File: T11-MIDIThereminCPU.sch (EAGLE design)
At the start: 62 parts, among them IC1 UA78M05DCY, IC4 QUAD_OPAMPD, IC5 4069D, J1 DCJ0202, Q1 16MHz, U1 ATMEGA328P-AU

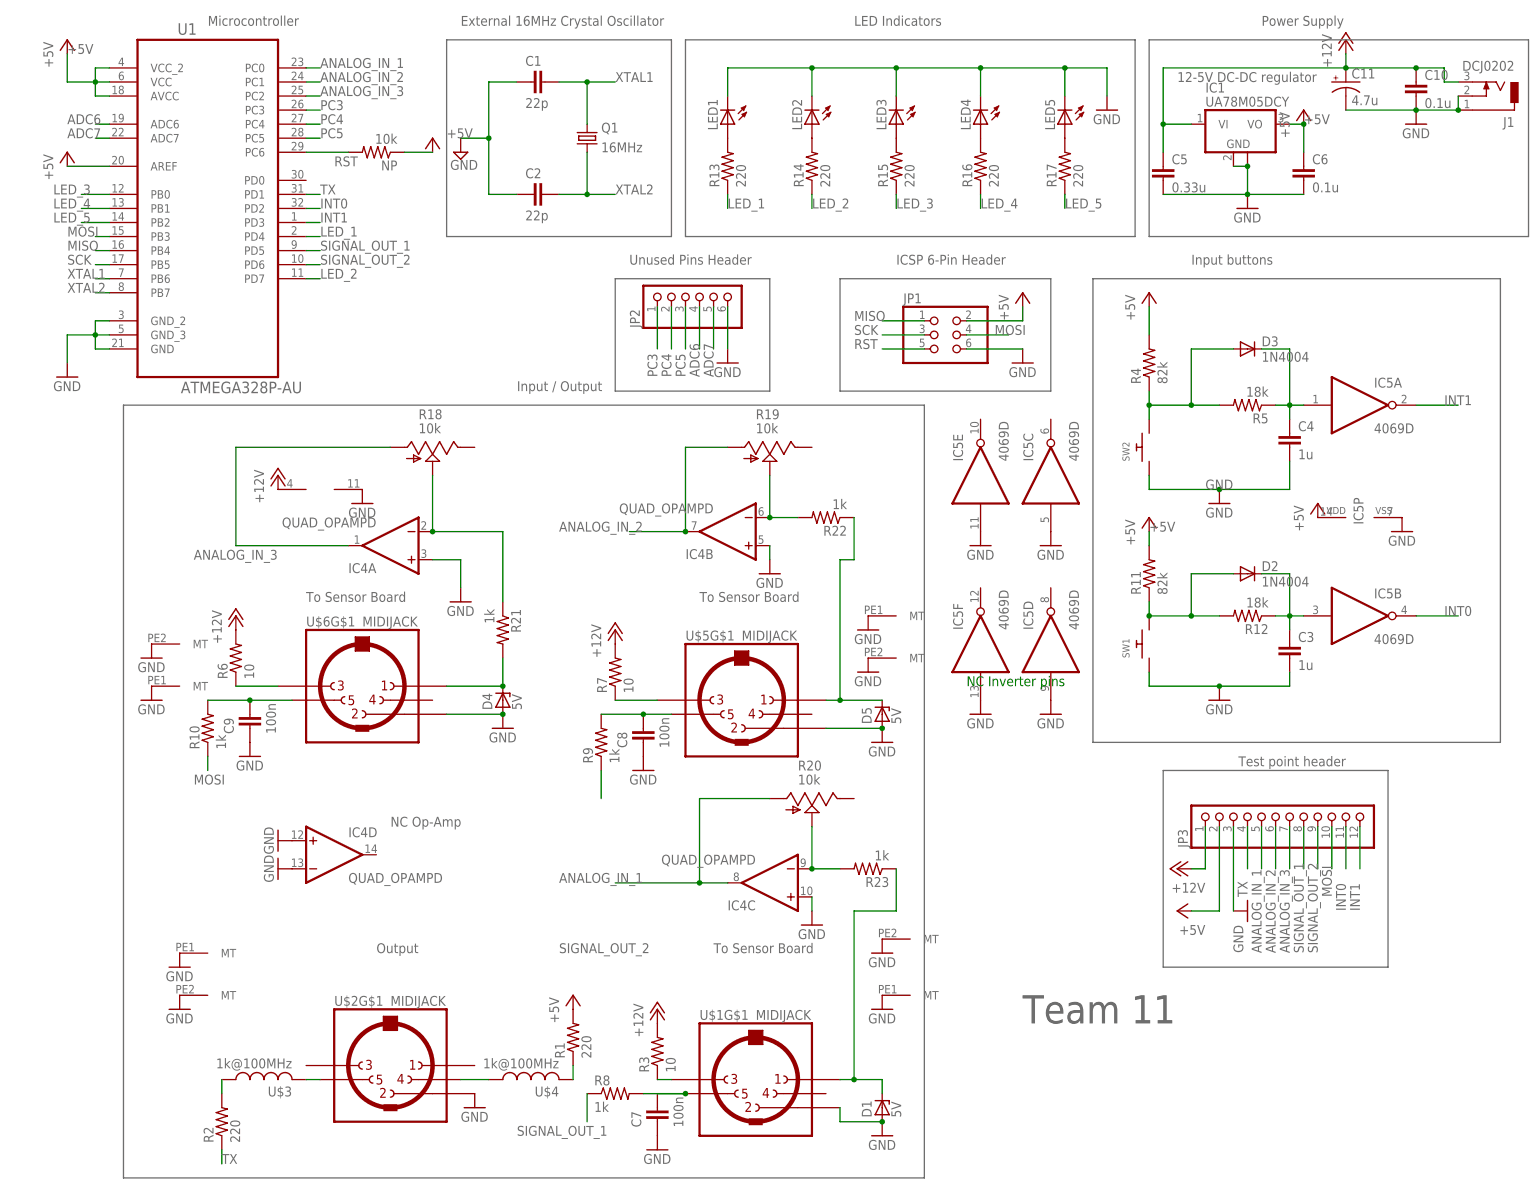
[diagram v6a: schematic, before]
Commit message: Changed resistors and caps to smd
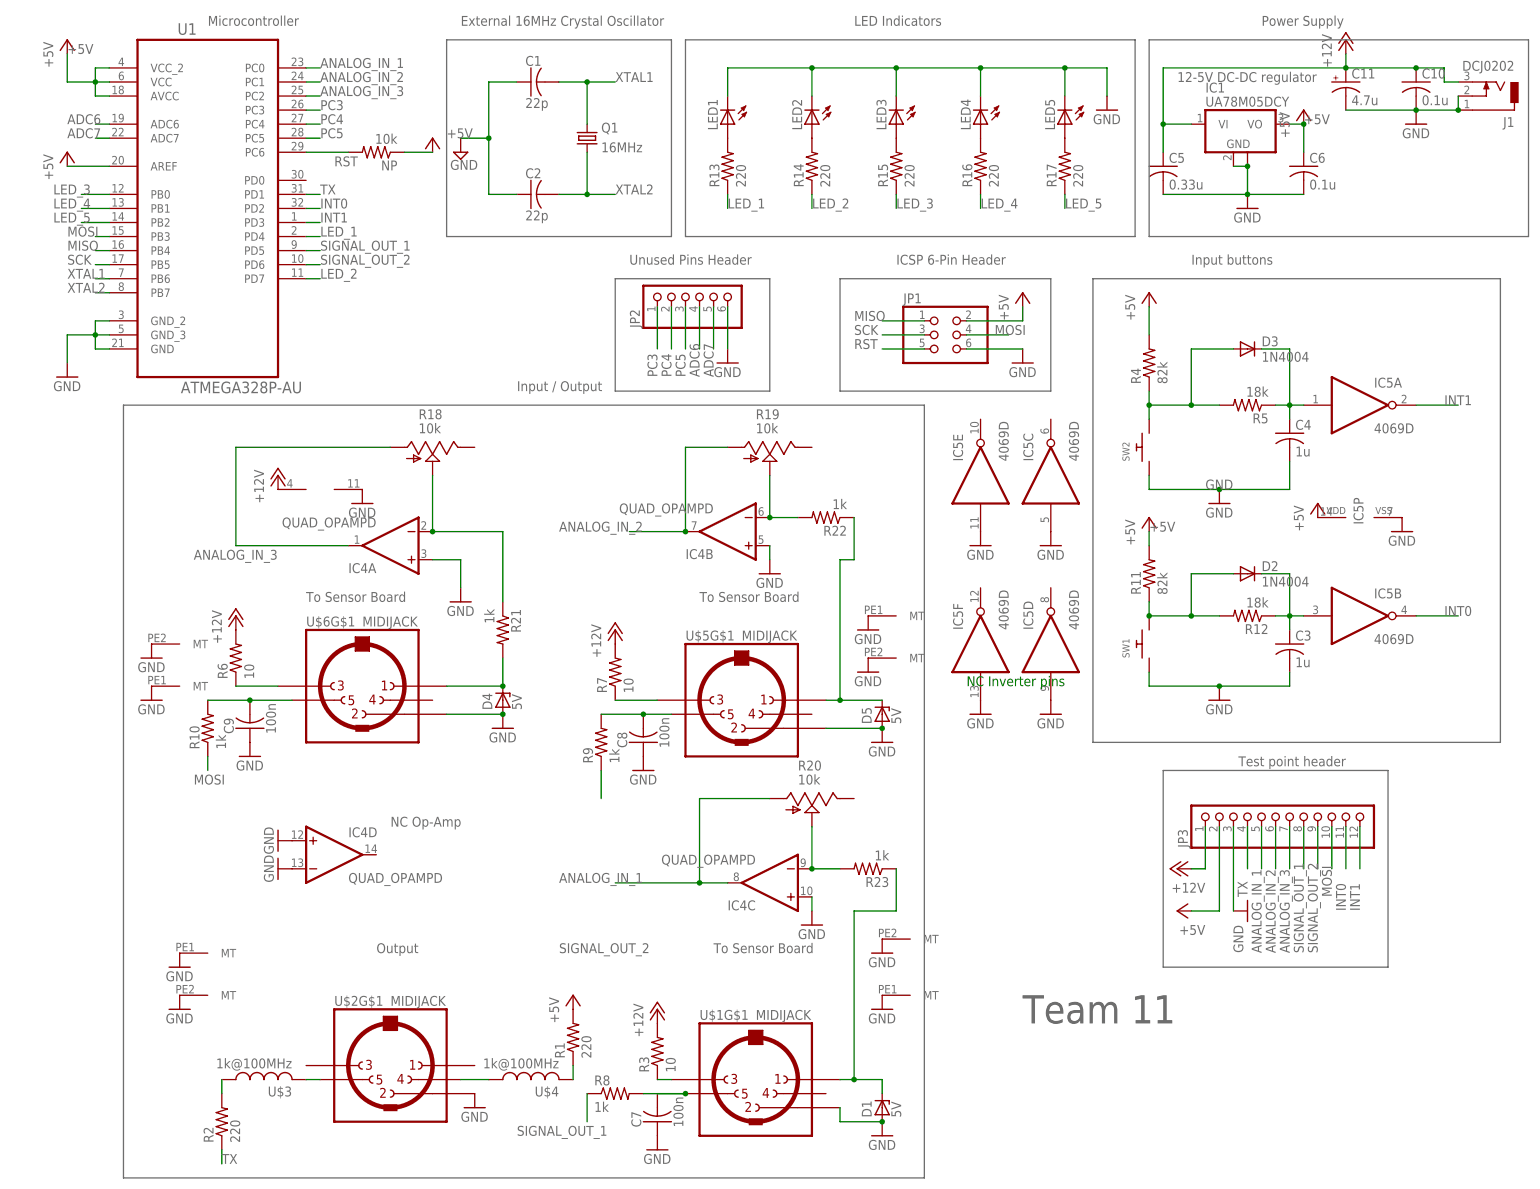
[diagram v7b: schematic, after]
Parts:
- C1, C10, C2, C3, C4, C5, C6, C7, C8, C9: device capacitor-wima:C2,5-3 -> adafruit:C-USC0805
- NP, R1, R11, R12, R13, R14, R15, R16, R17, R21, R22, R23, R3, R4, R5, R7, R8, R9: device resistor:R-US_0207/10 -> resistor:R-US_R0805
- R10, R2, R6: device resistor:R-US_0207/10 -> resistor:R-US_M0805
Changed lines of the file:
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@@
 <part name="U1" library="Atmel_By_element14_Batch_1-00" deviceset="ATMEGA328P-AU" device=""/>
 <part name="Q1" library="crystal" deviceset="CRYSTAL" device="SM49" value="16MHz"/>
-<part name="C1" library="capacitor-wima" deviceset="C" device="2,5-3" value="22p"/>
-<part name="C2" library="capacitor-wima" deviceset="C" device="2,5-3" value="22p"/>
+<part name="C1" library="adafruit" deviceset="C-US" device="C0805" value="22p"/>
+<part name="C2" library="adafruit" deviceset="C-US" device="C0805" value="22p"/>
 <part name="SUPPLY1" library="supply2" deviceset="GND" device=""/>
 <part name="JP1" library="pinhead" deviceset="PINHD-2X3" device=""/>
 <part name="IC1" library="linear" deviceset="UA78M*" device="DCY" technology="05"/>
 <part name="J1" library="con-jack" deviceset="DCJ0202" device=""/>
-<part name="C5" library="capacitor-wima" deviceset="C" device="2,5-3" value="0.33u"/>
-<part name="C6" library="capacitor-wima" deviceset="C" device="2,5-3" value="0.1u"/>
+<part name="C5" library="adafruit" deviceset="C-US" device="C0805" value="0.33u"/>
+<part name="C6" library="adafruit" deviceset="C-US" device="C0805" value="0.1u"/>
 <part name="U$1" library="adafruit" deviceset="MIDIJACK" device=""/>
 <part name="U$2" library="adafruit" deviceset="MIDIJACK" device=""/>
-<part name="R1" library="resistor" deviceset="R-US_" device="0207/10" value="220"/>
-<part name="R2" library="resistor" deviceset="R-US_" device="0207/10" value="220"/>
+<part name="R1" library="resistor" deviceset="R-US_" device="R0805" value="220"/>
+<part name="R2" library="resistor" deviceset="R-US_" device="M0805" value="220"/>
 <part name="D1" library="diode" deviceset="ZENER-DIODE" device="DO35Z10" value="5V"/>
-<part name="R3" library="resistor" deviceset="R-US_" device="0207/10" value="10"/>
+<part name="R3" library="resistor" deviceset="R-US_" device="R0805" value="10"/>
 <part name="SW1" library="adafruit" deviceset="SWITCH_PUSHBUTTON" device="SOFTTOUCHSMD_SJ"/>
-<part name="R11" library="resistor" deviceset="R-US_" device="0207/10" value="82k"/>
-<part name="R12" library="resistor" deviceset="R-US_" device="0207/10" value="18k"/>
-<part name="C3" library="capacitor-wima" deviceset="C" device="2,5-3" value="1u"/>
+<part name="R11" library="resistor" deviceset="R-US_" device="R0805" value="82k"/>
+<part name="R12" library="resistor" deviceset="R-US_" device="R0805" value="18k"/>
+<part name="C3" library="adafruit" deviceset="C-US" device="C0805" value="1u"/>
 <part name="D2" library="diode" deviceset="1N4004" device=""/>
 <part name="U$3" library="adafruit" deviceset="FB" device="" value="1k@100MHz"/>
 <part name="U$4" library="adafruit" deviceset="FB" device="" value="1k@100MHz"/>
-<part name="R4" library="resistor" deviceset="R-US_" device="0207/10" value="82k"/>
+<part name="R4" library="resistor" deviceset="R-US_" device="R0805" value="82k"/>
 <part name="SW2" library="adafruit" deviceset="SWITCH_PUSHBUTTON" device="SOFTTOUCHSMD_SJ"/>
-<part name="R5" library="resistor" deviceset="R-US_" device="0207/10" value="18k"/>
+<part name="R5" library="resistor" deviceset="R-US_" device="R0805" value="18k"/>
 <part name="D3" library="diode" deviceset="1N4004" device=""/>
-<part name="C4" library="capacitor-wima" deviceset="C" device="2,5-3" value="1u"/>
+<part name="C4" library="adafruit" deviceset="C-US" device="C0805" value="1u"/>
 <part name="U$5" library="adafruit" deviceset="MIDIJACK" device=""/>
 <part name="U$6" library="adafruit" deviceset="MIDIJACK" device=""/>
-<part name="R6" library="resistor" deviceset="R-US_" device="0207/10" value="10"/>
+<part name="R6" library="resistor" deviceset="R-US_" device="M0805" value="10"/>
 <part name="D4" library="diode" deviceset="ZENER-DIODE" device="DO35Z10" value="5V"/>
 <part name="D5" library="diode" deviceset="ZENER-DIODE" device="DO35Z10" value="5V"/>
-<part name="R7" library="resistor" deviceset="R-US_" device="0207/10" value="10"/>
-<part name="R8" library="resistor" deviceset="R-US_" device="0207/10" value="1k"/>
-<part name="C7" library="capacitor-wima" deviceset="C" device="2,5-3" value="100n"/>
-<part name="R9" library="resistor" deviceset="R-US_" device="0207/10" value="1k"/>
-<part name="C8" library="capacitor-wima" deviceset="C" device="2,5-3" value="100n"/>
-<part name="R10" library="resistor" deviceset="R-US_" device="0207/10" value="1k"/>
-<part name="C9" library="capacitor-wima" deviceset="C" device="2,5-3" value="100n"/>
+<part name="R7" library="resistor" deviceset="R-US_" device="R0805" value="10"/>
+<part name="R8" library="resistor" deviceset="R-US_" device="R0805" value="1k"/>
+<part name="C7" library="adafruit" deviceset="C-US" device="C0805" value="100n"/>
+<part name="R9" library="resistor" deviceset="R-US_" device="R0805" value="1k"/>
+<part name="C8" library="adafruit" deviceset="C-US" device="C0805" value="100n"/>
+<part name="R10" library="resistor" deviceset="R-US_" device="M0805" value="1k"/>
+<part name="C9" library="adafruit" deviceset="C-US" device="C0805" value="100n"/>
 <part name="LED1" library="adafruit" deviceset="LED" device="3MM"/>
 <part name="LED2" library="adafruit" deviceset="LED" device="3MM"/>
@@
 <part name="LED4" library="adafruit" deviceset="LED" device="3MM"/>
 <part name="LED5" library="adafruit" deviceset="LED" device="3MM"/>
-<part name="R13" library="resistor" deviceset="R-US_" device="0207/10" value="220"/>
-<part name="R14" library="resistor" deviceset="R-US_" device="0207/10" value="220"/>
-<part name="R15" library="resistor" deviceset="R-US_" device="0207/10" value="220"/>
-<part name="R16" library="resistor" deviceset="R-US_" device="0207/10" value="220"/>
-<part name="R17" library="resistor" deviceset="R-US_" device="0207/10" value="220"/>
-<part name="C10" library="capacitor-wima" deviceset="C" device="2,5-3" value="0.1u"/>
+<part name="R13" library="resistor" deviceset="R-US_" device="R0805" value="220"/>
+<part name="R14" library="resistor" deviceset="R-US_" device="R0805" value="220"/>
+<part name="R15" library="resistor" deviceset="R-US_" device="R0805" value="220"/>
+<part name="R16" library="resistor" deviceset="R-US_" device="R0805" value="220"/>
+<part name="R17" library="resistor" deviceset="R-US_" device="R0805" value="220"/>
+<part name="C10" library="adafruit" deviceset="C-US" device="C0805" value="0.1u"/>
 <part name="C11" library="adafruit" deviceset="CPOL-US" device="E3.5-8" value="4.7u"/>
 <part name="JP2" library="adafruit" deviceset="PINHD-1X6" device=""/>
-<part name="NP" library="resistor" deviceset="R-US_" device="0207/10" value="10k"/>
+<part name="NP" library="resistor" deviceset="R-US_" device="R0805" value="10k"/>
 <part name="JP3" library="adafruit" deviceset="PINHD-1X12" device=""/>
 <part name="P+1" library="supply1" deviceset="+5V" device=""/>
@@
 <part name="R19" library="pot" deviceset="TRIM_US-" device="B25U" value="10k"/>
 <part name="R20" library="pot" deviceset="TRIM_US-" device="B25U" value="10k"/>
-<part name="R21" library="resistor" deviceset="R-US_" device="0207/10" value="1k"/>
-<part name="R22" library="resistor" deviceset="R-US_" device="0207/10" value="1k"/>
-<part name="R23" library="resistor" deviceset="R-US_" device="0207/10" value="1k"/>
+<part name="R21" library="resistor" deviceset="R-US_" device="R0805" value="1k"/>
+<part name="R22" library="resistor" deviceset="R-US_" device="R0805" value="1k"/>
+<part name="R23" library="resistor" deviceset="R-US_" device="R0805" value="1k"/>
 <part name="GND27" library="supply1" deviceset="GND" device=""/>
 <part name="GND28" library="supply1" deviceset="GND" device=""/>

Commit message: Improved routing, coupling caps added
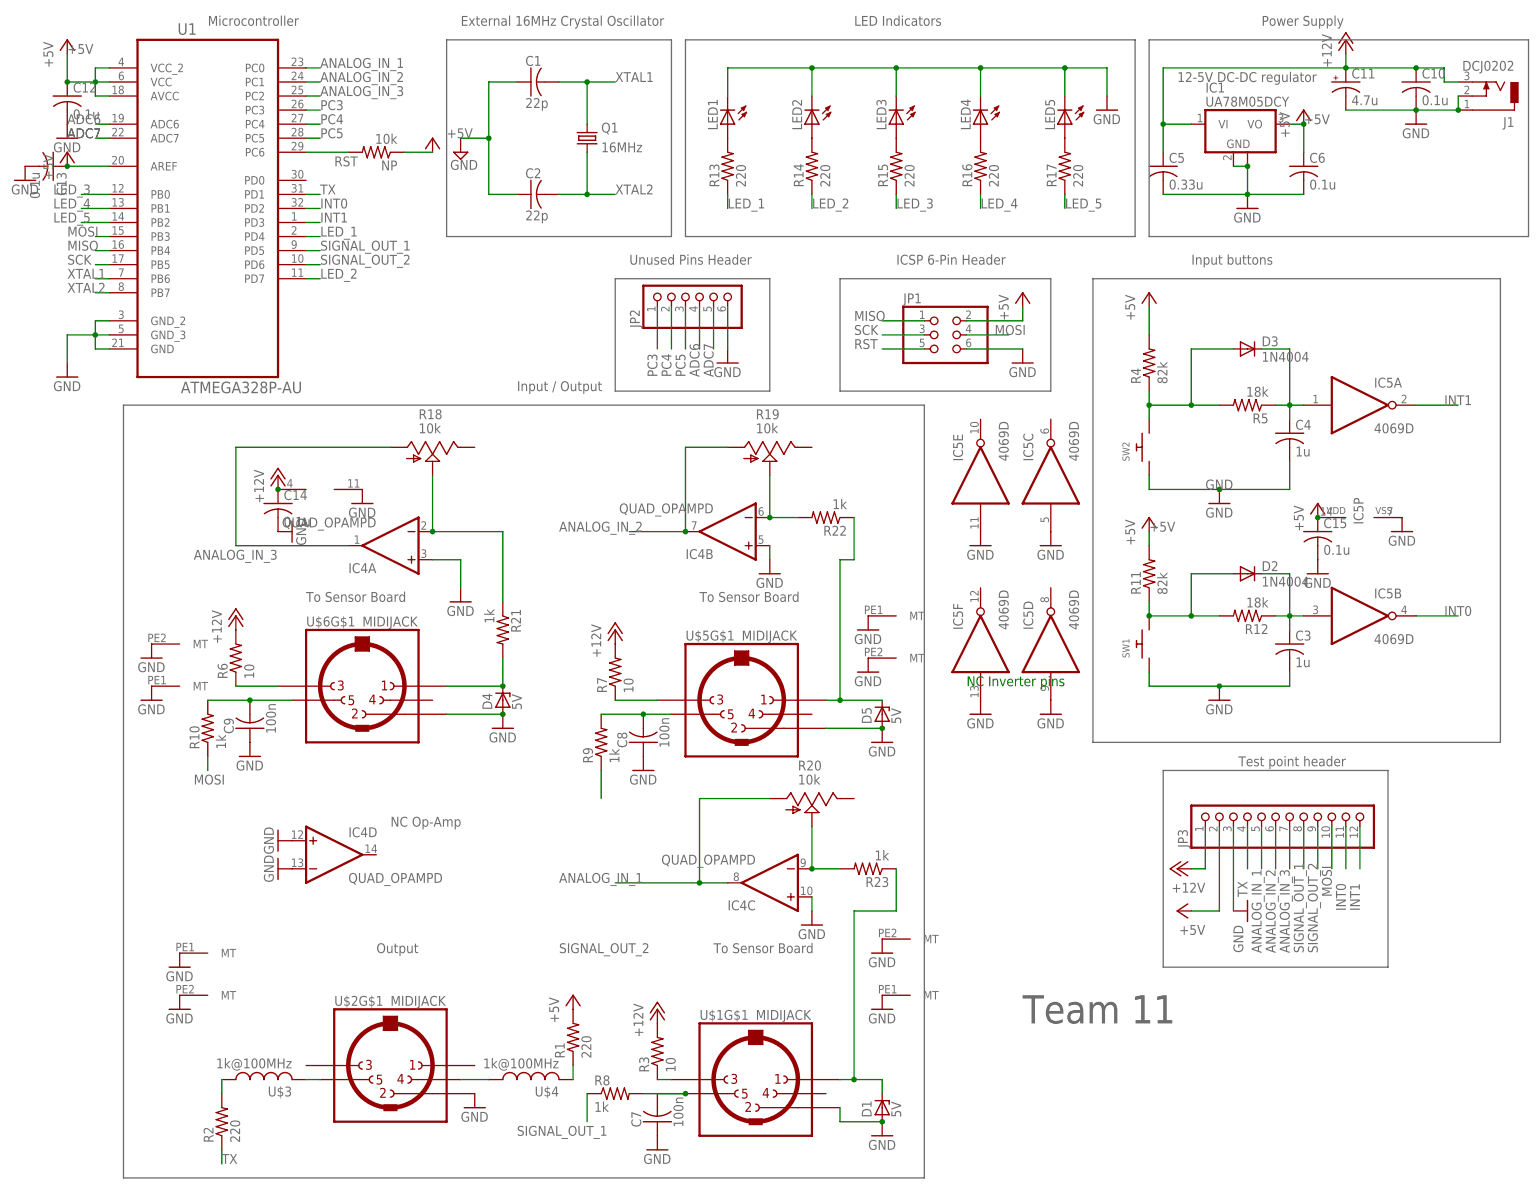
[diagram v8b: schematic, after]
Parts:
- added C12, C13, C14, C15: 0.1u, adafruit:C-USC0805
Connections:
- net +12V: now also C14.1
- net +5V: now also C12.1, C13.1, C15.1
- net GND: now also C12.2, C13.2, C14.2, C15.2
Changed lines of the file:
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@@
 <?xml version="1.0" encoding="utf-8"?>
 <!DOCTYPE eagle SYSTEM "eagle.dtd">
-<eagle version="7.6.0">
+<eagle version="7.5.0">
 <drawing>
 <settings>
@@
 <part name="GND34" library="supply1" deviceset="GND" device=""/>
 <part name="GND35" library="supply1" deviceset="GND" device=""/>
+<part name="C12" library="adafruit" deviceset="C-US" device="C0805" value="0.1u"/>
+<part name="GND36" library="supply1" deviceset="GND" device=""/>
+<part name="C13" library="adafruit" deviceset="C-US" device="C0805" value="0.1u"/>
+<part name="GND37" library="supply1" deviceset="GND" device=""/>
+<part name="C14" library="adafruit" deviceset="C-US" device="C0805" value="0.1u"/>
+<part name="C15" library="adafruit" deviceset="C-US" device="C0805" value="0.1u"/>
+<part name="GND38" library="supply1" deviceset="GND" device=""/>
+<part name="GND39" library="supply1" deviceset="GND" device=""/>
 </parts>
 <sheets>
@@
 <instance part="GND34" gate="1" x="48.26" y="60.96" rot="R270"/>
 <instance part="GND35" gate="1" x="48.26" y="55.88" rot="R270"/>
+<instance part="C12" gate="G$1" x="10.16" y="195.58"/>
+<instance part="GND36" gate="1" x="10.16" y="187.96"/>
+<instance part="C13" gate="G$1" x="7.62" y="182.88" rot="R270"/>
+<instance part="GND37" gate="1" x="2.54" y="180.34"/>
+<instance part="C14" gate="G$1" x="48.26" y="121.92"/>
+<instance part="C15" gate="G$1" x="236.22" y="116.84"/>
+<instance part="GND38" gate="1" x="236.22" y="109.22"/>
+<instance part="GND39" gate="1" x="50.8" y="116.84" rot="R90"/>
 </instances>
 <busses>
@@
 <pinref part="GND35" gate="1" pin="GND"/>
 </segment>
+<segment>
+<pinref part="C12" gate="G$1" pin="2"/>
+<pinref part="GND36" gate="1" pin="GND"/>
+</segment>
+<segment>
+<pinref part="C13" gate="G$1" pin="2"/>
+<pinref part="GND37" gate="1" pin="GND"/>
+</segment>
+<segment>
+<pinref part="C15" gate="G$1" pin="2"/>
+<pinref part="GND38" gate="1" pin="GND"/>
+</segment>
+<segment>
+<pinref part="C14" gate="G$1" pin="2"/>
+<pinref part="GND39" gate="1" pin="GND"/>
+</segment>
 </net>
 <net name="MISO" class="0">
@@
 <wire x1="10.16" y1="198.12" x2="10.16" y2="203.2" width="0.1524" layer="91"/>
 <pinref part="P+1" gate="1" pin="+5V"/>
+<pinref part="C12" gate="G$1" pin="1"/>
+<junction x="10.16" y="198.12"/>
 </segment>
 <segment>
@@
 <pinref part="P+12" gate="1" pin="+5V"/>
 <wire x1="17.78" y1="182.88" x2="10.16" y2="182.88" width="0.1524" layer="91"/>
+<pinref part="C13" gate="G$1" pin="1"/>
+<junction x="10.16" y="182.88"/>
 </segment>
 <segment>
@@
 <pinref part="IC5" gate="P" pin="VDD"/>
 <pinref part="P+5" gate="1" pin="+5V"/>
+<pinref part="C15" gate="G$1" pin="1"/>
+<junction x="236.22" y="119.38"/>
+<pinref part="C15" gate="G$1" pin="1"/>
 </segment>
 </net>
@@
 <pinref part="IC4" gate="P" pin="V+"/>
 <pinref part="P+17" gate="1" pin="+12V"/>
+<pinref part="C14" gate="G$1" pin="1"/>
+<junction x="48.26" y="124.46"/>
+<pinref part="C14" gate="G$1" pin="1"/>
 </segment>
 </net>
@@
 <wire x1="17.78" y1="187.96" x2="15.24" y2="187.96" width="0.1524" layer="91"/>
 <label x="10.16" y="187.96" size="1.778" layer="95" font="fixed"/>
-</segment>
+<label x="10.16" y="187.96" size="1.778" layer="95" font="fixed"/>
+</segment>
